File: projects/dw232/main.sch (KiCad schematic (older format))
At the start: 0 parts

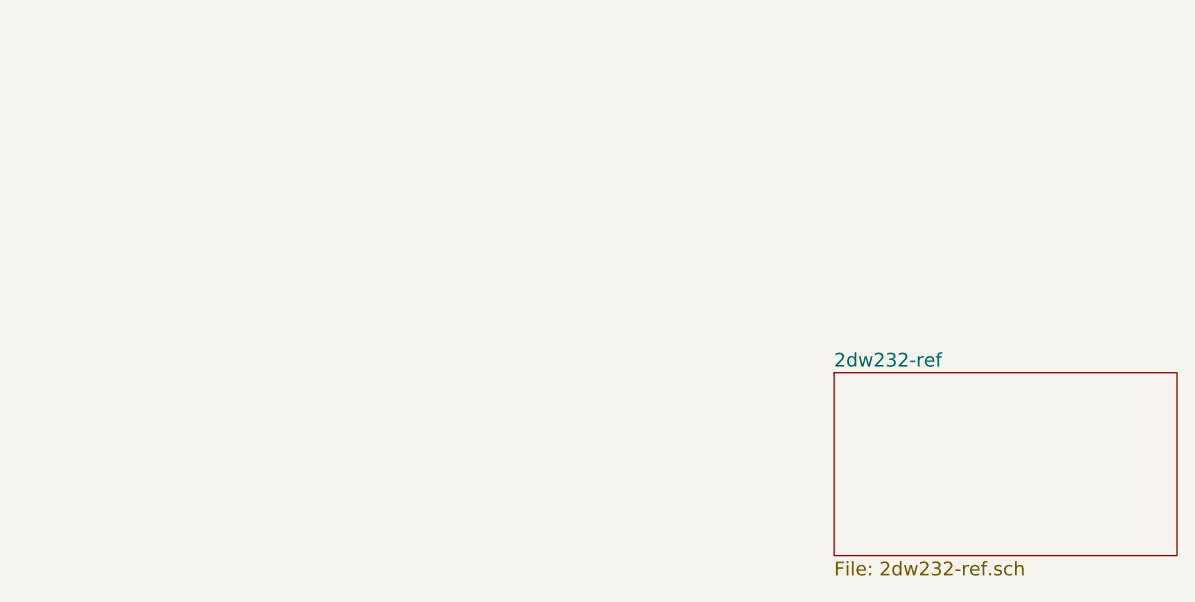
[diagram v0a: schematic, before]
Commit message: remove old stuff for reference
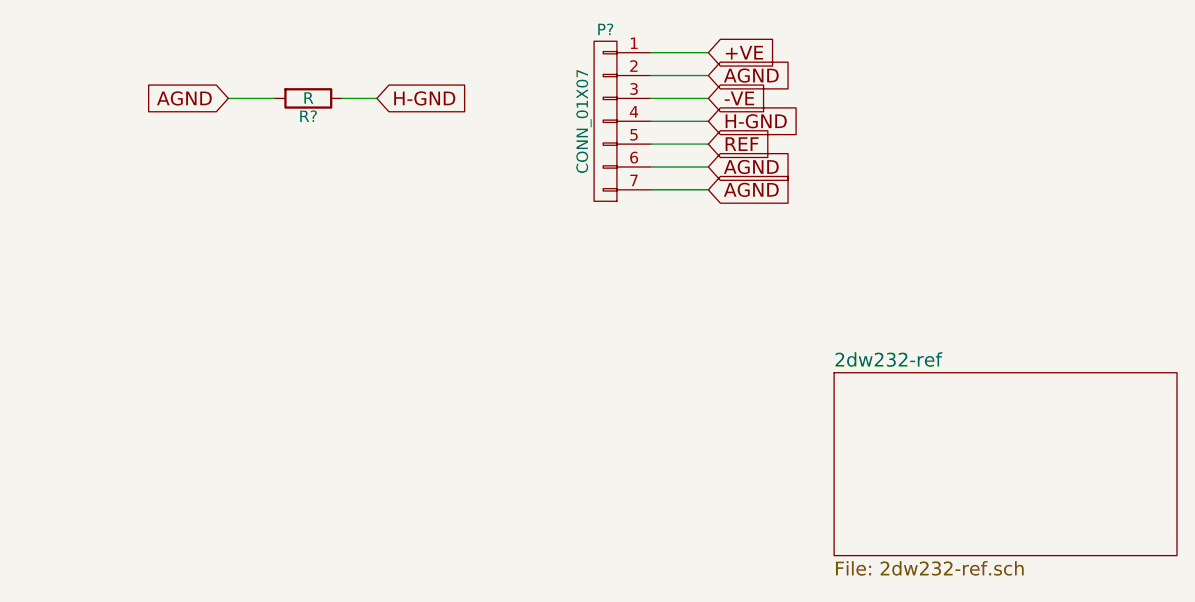
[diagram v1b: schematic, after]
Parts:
- added P?: CONN_01X07, Pin_Headers:Pin_Header_Straight_1x07, symbol CONN_01X07
- added R?: R, Resistors_SMD:R_1206, symbol R
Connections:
- new net +VE: P?.1 (P1)
- new net -VE: P?.3 (P3)
- new net AGND: P?.2 (P2), P?.6 (P6), P?.7 (P7), R?.2
- new net H-GND: P?.4 (P4), R?.1
- new net REF: P?.5 (P5)
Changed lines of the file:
@@
 $Descr A4 11693 8268
 encoding utf-8
-Sheet 1 4
+Sheet 1 2
 Title ""
 Date ""
@@
 F1 "2dw232-ref.sch" 60
 $EndSheet
+$Comp
+L CONN_01X07 P?
+U 1 1 58A3916C
+P 4200 1750
+F 0 "P?" H 4200 2150 50  0000 C CNN
+F 1 "CONN_01X07" V 4300 1750 50  0000 C CNN
+F 2 "Pin_Headers:Pin_Header_Straight_1x07" H 4200 1750 50  0001 C CNN
+F 3 "" H 4200 1750 50  0000 C CNN
+	1    4200 1750
+	-1   0    0    -1
+$EndComp
+Text GLabel 4650 1450 2    60   Input ~ 0
++VE
+Wire Wire Line
+	4400 1450 4650 1450
+Text GLabel 4650 1550 2    60   Input ~ 0
+AGND
+Wire Wire Line
+	4400 1550 4650 1550
+Text GLabel 4650 1850 2    60   Input ~ 0
+REF
+Text GLabel 4650 1950 2    60   Input ~ 0
+AGND
+Text GLabel 4650 2050 2    60   Input ~ 0
+AGND
+Wire Wire Line
+	4400 1950 4650 1950
+Wire Wire Line
+	4400 2050 4650 2050
+Text GLabel 4650 1650 2    60   Input ~ 0
+-VE
+Wire Wire Line
+	4400 1650 4650 1650
+Text GLabel 4650 1750 2    60   Input ~ 0
+H-GND
+Wire Wire Line
+	4400 1750 4650 1750
+Wire Wire Line
+	4400 1850 4650 1850
+Text GLabel 3200 1650 2    60   Input ~ 0
+H-GND
+Text GLabel 2550 1650 0    60   Input ~ 0
+AGND
+$Comp
+L R R?
+U 1 1 58A39183
+P 2900 1650
+F 0 "R?" V 2980 1650 50  0000 C CNN
+F 1 "R" V 2900 1650 50  0000 C CNN
+F 2 "Resistors_SMD:R_1206" V 2830 1650 50  0001 C CNN
+F 3 "" H 2900 1650 50  0000 C CNN
+	1    2900 1650
+	0    1    1    0
+$EndComp
+Wire Wire Line
+	2550 1650 2750 1650
+Wire Wire Line
+	3050 1650 3200 1650
 $EndSCHEMATC

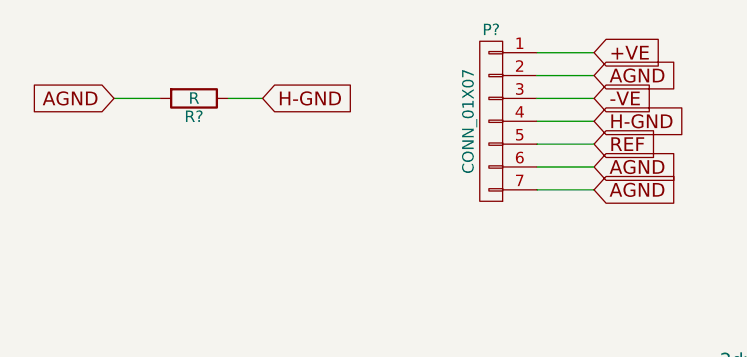
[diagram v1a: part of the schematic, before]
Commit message: change trimmers to fixed resistors
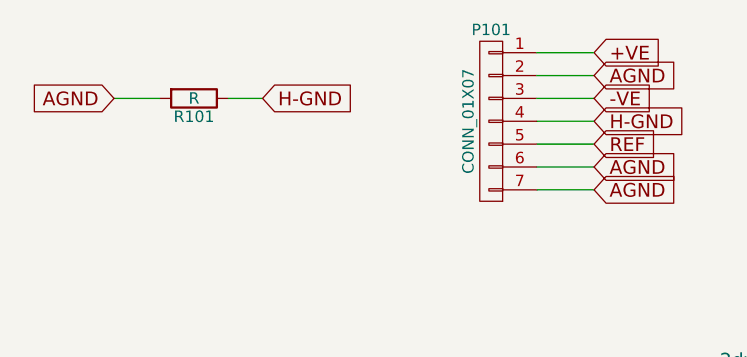
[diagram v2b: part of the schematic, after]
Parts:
- gave numbers to parts that had none: 2
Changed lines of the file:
@@
 $EndSheet
 $Comp
-L CONN_01X07 P?
+L CONN_01X07 P101
 U 1 1 58A3916C
 P 4200 1750
-F 0 "P?" H 4200 2150 50  0000 C CNN
+F 0 "P101" H 4200 2150 50  0000 C CNN
 F 1 "CONN_01X07" V 4300 1750 50  0000 C CNN
 F 2 "Pin_Headers:Pin_Header_Straight_1x07" H 4200 1750 50  0001 C CNN
@@
 AGND
 $Comp
-L R R?
+L R R101
 U 1 1 58A39183
 P 2900 1650
-F 0 "R?" V 2980 1650 50  0000 C CNN
+F 0 "R101" V 2980 1650 50  0000 C CNN
 F 1 "R" V 2900 1650 50  0000 C CNN
 F 2 "Resistors_SMD:R_1206" V 2830 1650 50  0001 C CNN

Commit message: v0.2 2dw232
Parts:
- removed P101: CONN_01X07, Pin_Headers:Pin_Header_Straight_1x07, symbol CONN_01X07
- added P101: CONN_01X11, symbol CONN_01X11
- added R102, R103: 0R, symbol R
- R101: value R -> 0R
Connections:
- net +VE: now also P101.1 (P1)
- net -VE: now also P101.3 (P3), R102.1
- net AGND: now also P101.10 (P10), P101.11 (P11), P101.2 (P2), R102.2, R103.2
- net H-GND: now also P101.4 (P4)
- new net T-SENSE: P101.8 (P8)
- new net T-SET: P101.9 (P9)
- new net V-OUT: P101.5 (P5)
- new net Z-SENSE: P101.6 (P6)
- new net Z-SENSE-GND: P101.7 (P7), R103.1
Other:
- moved on the sheet: R101
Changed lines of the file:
@@
 F1 "2dw232-ref.sch" 60
 $EndSheet
-$Comp
-L CONN_01X07 P101
-U 1 1 58A3916C
-P 4200 1750
-F 0 "P101" H 4200 2150 50  0000 C CNN
-F 1 "CONN_01X07" V 4300 1750 50  0000 C CNN
-F 2 "Pin_Headers:Pin_Header_Straight_1x07" H 4200 1750 50  0001 C CNN
-F 3 "" H 4200 1750 50  0000 C CNN
-	1    4200 1750
-	-1   0    0    -1
-$EndComp
 Text GLabel 4650 1450 2    60   Input ~ 0
 +VE
@@
 Wire Wire Line
 	4400 1550 4650 1550
+Text GLabel 4650 1950 2    60   Input ~ 0
+Z-SENSE
 Text GLabel 4650 1850 2    60   Input ~ 0
-REF
-Text GLabel 4650 1950 2    60   Input ~ 0
-AGND
-Text GLabel 4650 2050 2    60   Input ~ 0
-AGND
+V-OUT
+Text GLabel 4650 2150 2    60   Input ~ 0
+T-SENSE
 Wire Wire Line
-	4400 1950 4650 1950
-Wire Wire Line
-	4400 2050 4650 2050
+	4400 2150 4650 2150
 Text GLabel 4650 1650 2    60   Input ~ 0
 -VE
@@
 	4400 1750 4650 1750
 Wire Wire Line
-	4400 1850 4650 1850
-Text GLabel 3200 1650 2    60   Input ~ 0
+	4400 1950 4650 1950
+Text GLabel 2750 1500 2    60   Input ~ 0
 H-GND
-Text GLabel 2550 1650 0    60   Input ~ 0
+Text GLabel 2050 1500 0    60   Input ~ 0
 AGND
 $Comp
 L R R101
 U 1 1 58A39183
-P 2900 1650
-F 0 "R101" V 2980 1650 50  0000 C CNN
-F 1 "R" V 2900 1650 50  0000 C CNN
-F 2 "Resistors_SMD:R_1206" V 2830 1650 50  0001 C CNN
-F 3 "" H 2900 1650 50  0000 C CNN
-	1    2900 1650
+P 2400 1500
+F 0 "R101" V 2480 1500 50  0000 C CNN
+F 1 "0R" V 2400 1500 50  0000 C CNN
+F 2 "Resistors_SMD:R_1206" V 2330 1500 50  0001 C CNN
+F 3 "" H 2400 1500 50  0000 C CNN
+	1    2400 1500
 	0    1    1    0
 $EndComp
 Wire Wire Line
-	2550 1650 2750 1650
+	2050 1500 2250 1500
 Wire Wire Line
-	3050 1650 3200 1650
+	2550 1500 2750 1500
+$Comp
+L R R102
+U 1 1 58B28AD9
+P 2400 1900
+F 0 "R102" V 2480 1900 50  0000 C CNN
+F 1 "0R" V 2400 1900 50  0000 C CNN
+F 2 "" V 2330 1900 50  0000 C CNN
+F 3 "" H 2400 1900 50  0000 C CNN
+	1    2400 1900
+	0    1    1    0
+$EndComp
+Text GLabel 2750 1900 2    60   Input ~ 0
+-VE
+Wire Wire Line
+	2550 1900 2750 1900
+Text GLabel 2050 1900 0    60   Input ~ 0
+AGND
+Wire Wire Line
+	2050 1900 2250 1900
+Text GLabel 4650 2250 2    60   Input ~ 0
+T-SET
+Text GLabel 4650 2350 2    60   Input ~ 0
+AGND
+Text GLabel 4650 2450 2    60   Input ~ 0
+AGND
+$Comp
+L CONN_01X11 P101
+U 1 1 58B28D45
+P 4200 1950
+F 0 "P101" H 4200 2550 50  0000 C CNN
+F 1 "CONN_01X11" V 4300 1950 50  0000 C CNN
+F 2 "" H 4200 1950 50  0000 C CNN
+F 3 "" H 4200 1950 50  0000 C CNN
+	1    4200 1950
+	-1   0    0    -1
+$EndComp
+Wire Wire Line
+	4400 2250 4650 2250
+Wire Wire Line
+	4400 2350 4650 2350
+Wire Wire Line
+	4400 2450 4650 2450
+Text GLabel 4650 2050 2    60   Input ~ 0
+Z-SENSE-GND
+Wire Wire Line
+	4400 2050 4650 2050
+Wire Wire Line
+	4400 1850 4650 1850
+$Comp
+L R R103
+U 1 1 58B32019
+P 2400 2300
+F 0 "R103" V 2480 2300 50  0000 C CNN
+F 1 "0R" V 2400 2300 50  0000 C CNN
+F 2 "" V 2330 2300 50  0000 C CNN
+F 3 "" H 2400 2300 50  0000 C CNN
+	1    2400 2300
+	0    1    1    0
+$EndComp
+Text GLabel 2750 2300 2    60   Input ~ 0
+Z-SENSE-GND
+Wire Wire Line
+	2550 2300 2750 2300
+Text GLabel 2050 2300 0    60   Input ~ 0
+AGND
+Wire Wire Line
+	2050 2300 2250 2300
 $EndSCHEMATC

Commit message: update components
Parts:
- P101: footprint (none) -> Pin_Headers:Pin_Header_Straight_1x11
- R102, R103: footprint (none) -> Resistors_SMD:R_1206
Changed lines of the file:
@@
 F 0 "R102" V 2480 1900 50  0000 C CNN
 F 1 "0R" V 2400 1900 50  0000 C CNN
-F 2 "" V 2330 1900 50  0000 C CNN
+F 2 "Resistors_SMD:R_1206" V 2330 1900 50  0001 C CNN
 F 3 "" H 2400 1900 50  0000 C CNN
 	1    2400 1900
@@
 F 0 "P101" H 4200 2550 50  0000 C CNN
 F 1 "CONN_01X11" V 4300 1950 50  0000 C CNN
-F 2 "" H 4200 1950 50  0000 C CNN
+F 2 "Pin_Headers:Pin_Header_Straight_1x11" H 4200 1950 50  0001 C CNN
 F 3 "" H 4200 1950 50  0000 C CNN
 	1    4200 1950
@@
 F 0 "R103" V 2480 2300 50  0000 C CNN
 F 1 "0R" V 2400 2300 50  0000 C CNN
-F 2 "" V 2330 2300 50  0000 C CNN
+F 2 "Resistors_SMD:R_1206" V 2330 2300 50  0001 C CNN
 F 3 "" H 2400 2300 50  0000 C CNN
 	1    2400 2300
